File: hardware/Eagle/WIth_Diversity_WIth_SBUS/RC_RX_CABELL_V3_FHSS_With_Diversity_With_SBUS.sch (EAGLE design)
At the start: 19 parts, among them IC1 AMS1117 3V3, M2 NRF24L01

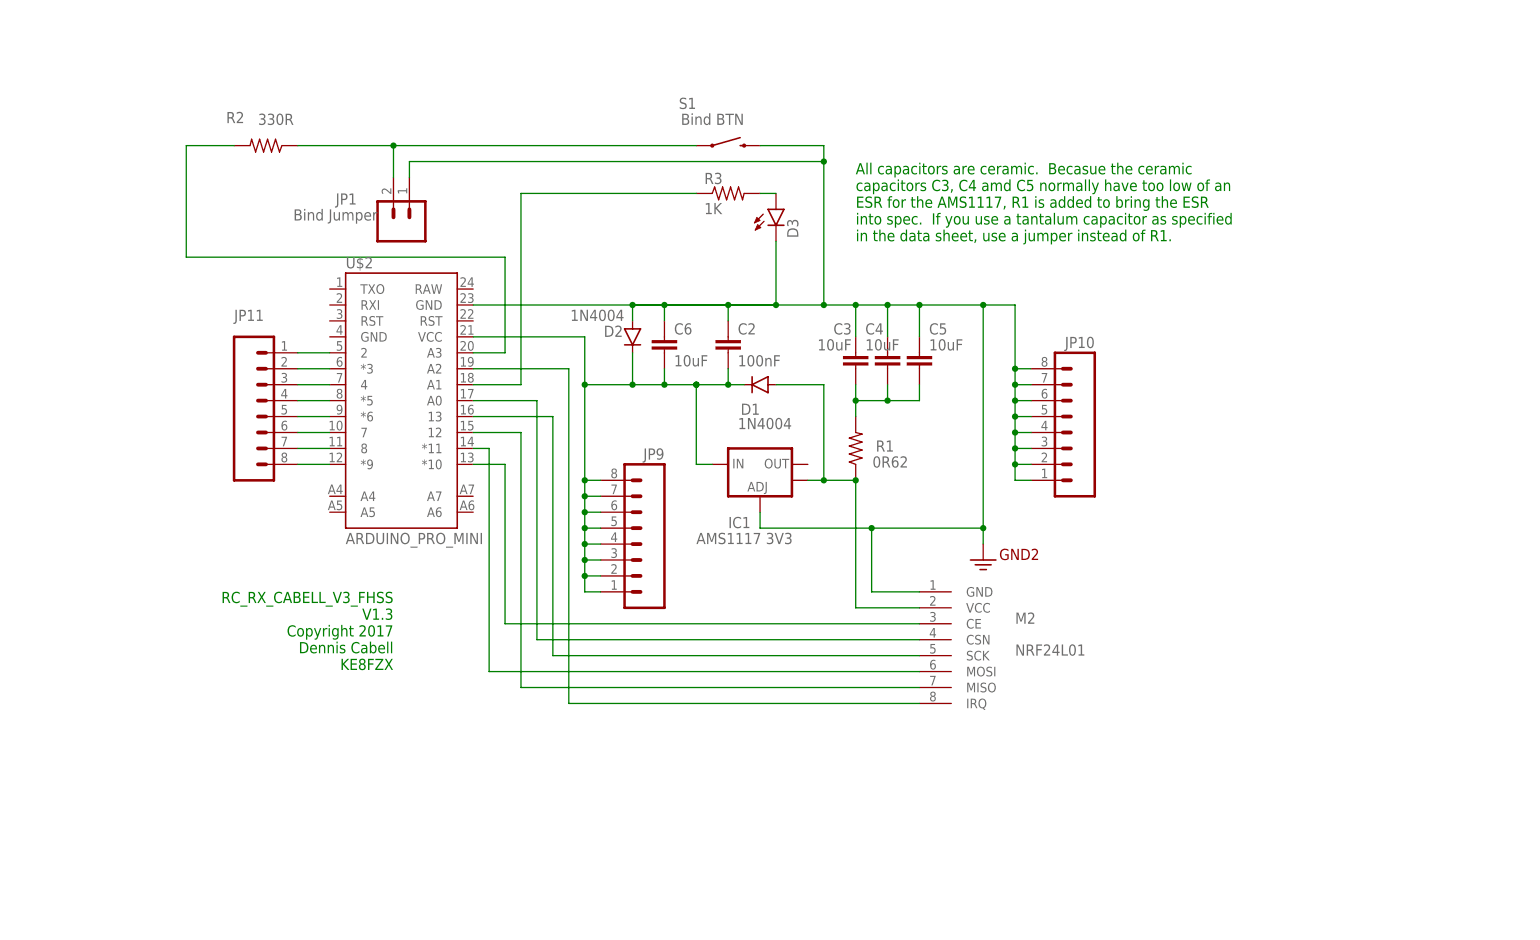
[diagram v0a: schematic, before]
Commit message: Hardware Updates for SBUS & PPM
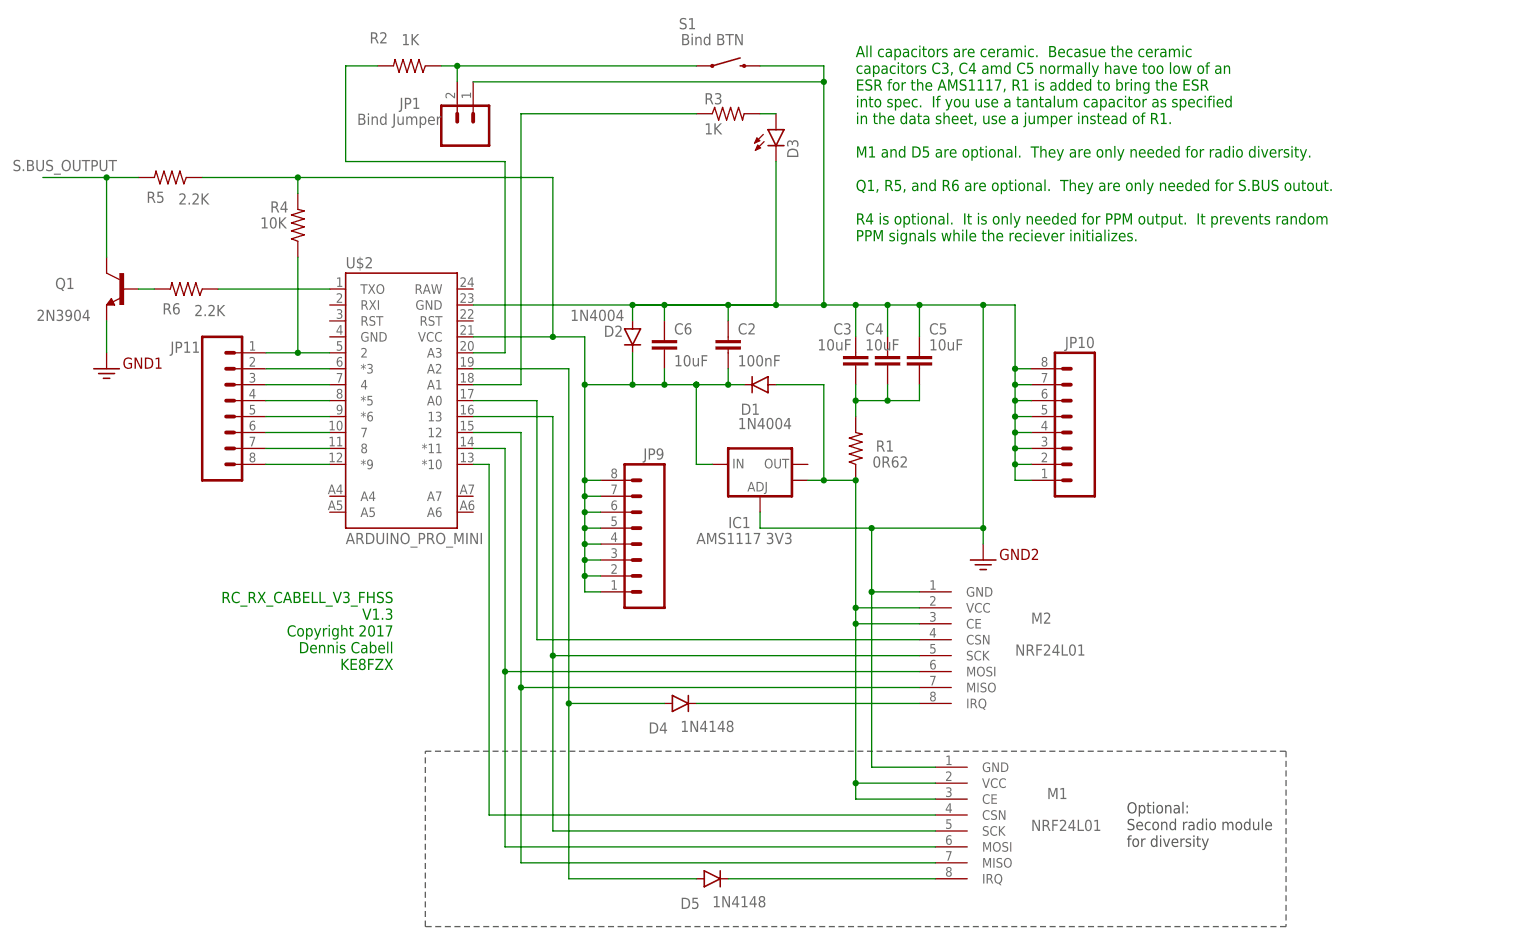
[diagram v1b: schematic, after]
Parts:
- added D4: 1N4148, SparkFun-DiscreteSemi:DIODE1N4148
- added D5: 1N4148, SparkFun-DiscreteSemi:DIODEPTH
- added M1: NRF24L01, diy-modules:WIRELESS-NRF24L01
- added Q1: 2N3904, SparkFun-DiscreteSemi:TRANSISTOR_NPN2N3904
- added R4: 10K, SparkFun-Passives:RESISTORAXIAL-0.3
- added R5, R6: 2.2K, SparkFun-Passives:RESISTORAXIAL-0.3
- R2: value 330R -> 1K
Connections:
- new net 3.3V: Q1.E
- new net N$16: D4.C, M2.IRQ
- new net N$17: D5.C, M1.IRQ
- new net N$23: M1.CSN, U$2.*10
- new net S.BUS_OUTPUT: Q1.C, R5.2
- new net SERIAL_SIG: Q1.B, R6.2
- net 5V: now also R4.2, R5.1
- net GND: now also M1.GND
- net N$1: now also R4.1
- net N$13: now also D4.A, D5.A; no longer M2.IRQ
- net N$15: now also M1.SCK
- net N$20: now also M1.MOSI
- net N$22: now also M1.MISO
- net N$3: now also R6.1, U$2.TXO; no longer M2.CE, U$2.*10
- net VCC: now also M1.CE, M1.VCC, M2.CE
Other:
- note added: "All capacitors are ceramic. Becasue the ceramic capacitors C3, C4 amd C5 normally have too low of an ESR for the AMS1117, R1 is added to bring the ESR into spec. If you use a tantalum capacitor as specified in the data sheet, use a jumper instead of R1. M1 and D5 are optional. They are only needed for radio diversity. Q1, R5, and R6 are optional. They are only needed for S.BUS outout. R4 is optio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"
- note added: "Optional: Second radio module for diversity"
- note removed: "All capacitors are ceramic. Becasue the ceramic capacitors C3, C4 amd C5 normally have too low of an ESR for the AMS1117, R1 is added to bring the ESR into spec. If you use a tantalum capacitor as specified in the data sheet, use a jumper instead of R1."
- moved on the sheet: D3, JP1, JP11, R2, R3, S1
